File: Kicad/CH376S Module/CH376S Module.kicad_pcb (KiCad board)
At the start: 2 copper layers, 52.1 x 29 mm, 14 parts, among them P1 HEADER, U1 CH376, U2 LM1117-3.3, Y2 12 MHz

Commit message: updates to 386
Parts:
- removed C3: 10uF, Capacitor_THT:C_Disc_D4.3mm_W1.9mm_P5.00mm
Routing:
- net /GND: track 86.8 -> 77.9 mm, vias 5 -> 4
- net /5+: track 66.7 -> 62.9 mm, vias 5 -> 4
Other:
- board text removed: "+"

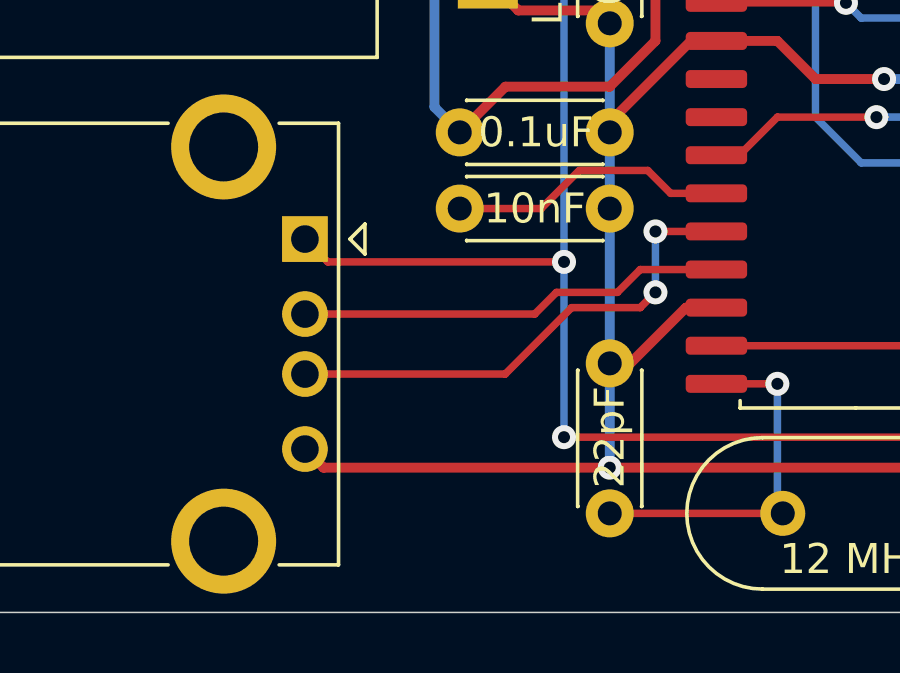
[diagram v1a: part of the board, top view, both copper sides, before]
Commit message: added 8088 card with ZIF socket
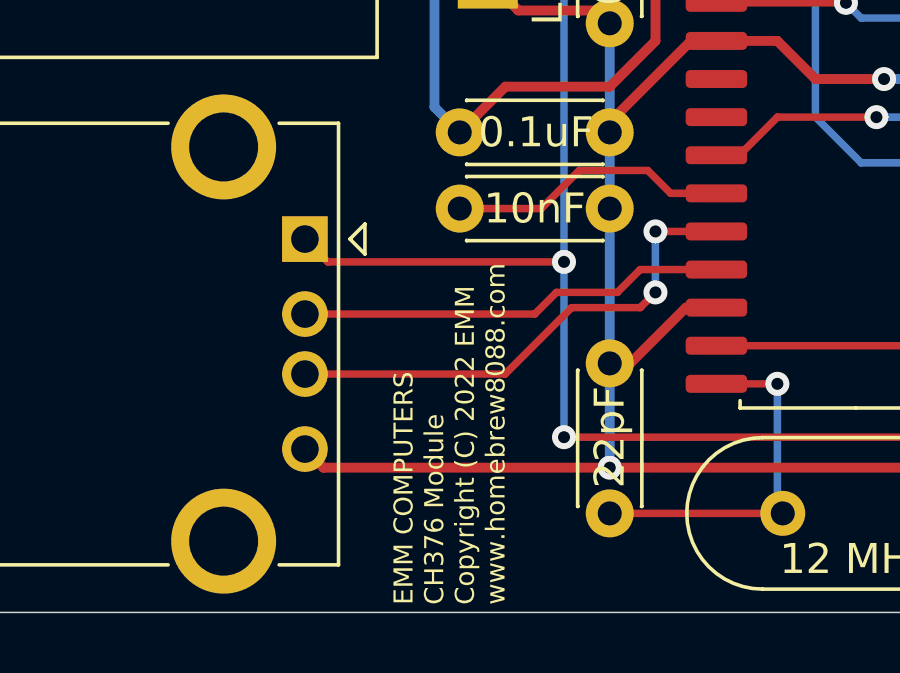
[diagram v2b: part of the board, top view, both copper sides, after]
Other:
- board text added: "EMM COMPUTERS CH376 Module Copyright (C) 2022 EMM www.homebrew8088.com"

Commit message: Updated Gerber's
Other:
- board text added: "EMM COMPUTERS CH376 Module Copyright (C) 2023 EMM www.homebrew8088.com"
- board text removed: "EMM COMPUTERS CH376 Module Copyright (C) 2022 EMM www.homebrew8088.com"
